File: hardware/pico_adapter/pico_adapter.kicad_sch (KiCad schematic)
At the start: 48 parts, among them J1 L77HDE15SD1CH4F, J2 AudioJack2_Ground, J3 Barrel_Jack, Q1 Q_NMOS_DGS, Q2 Q_NMOS_DGS, U1 DCDC-Module

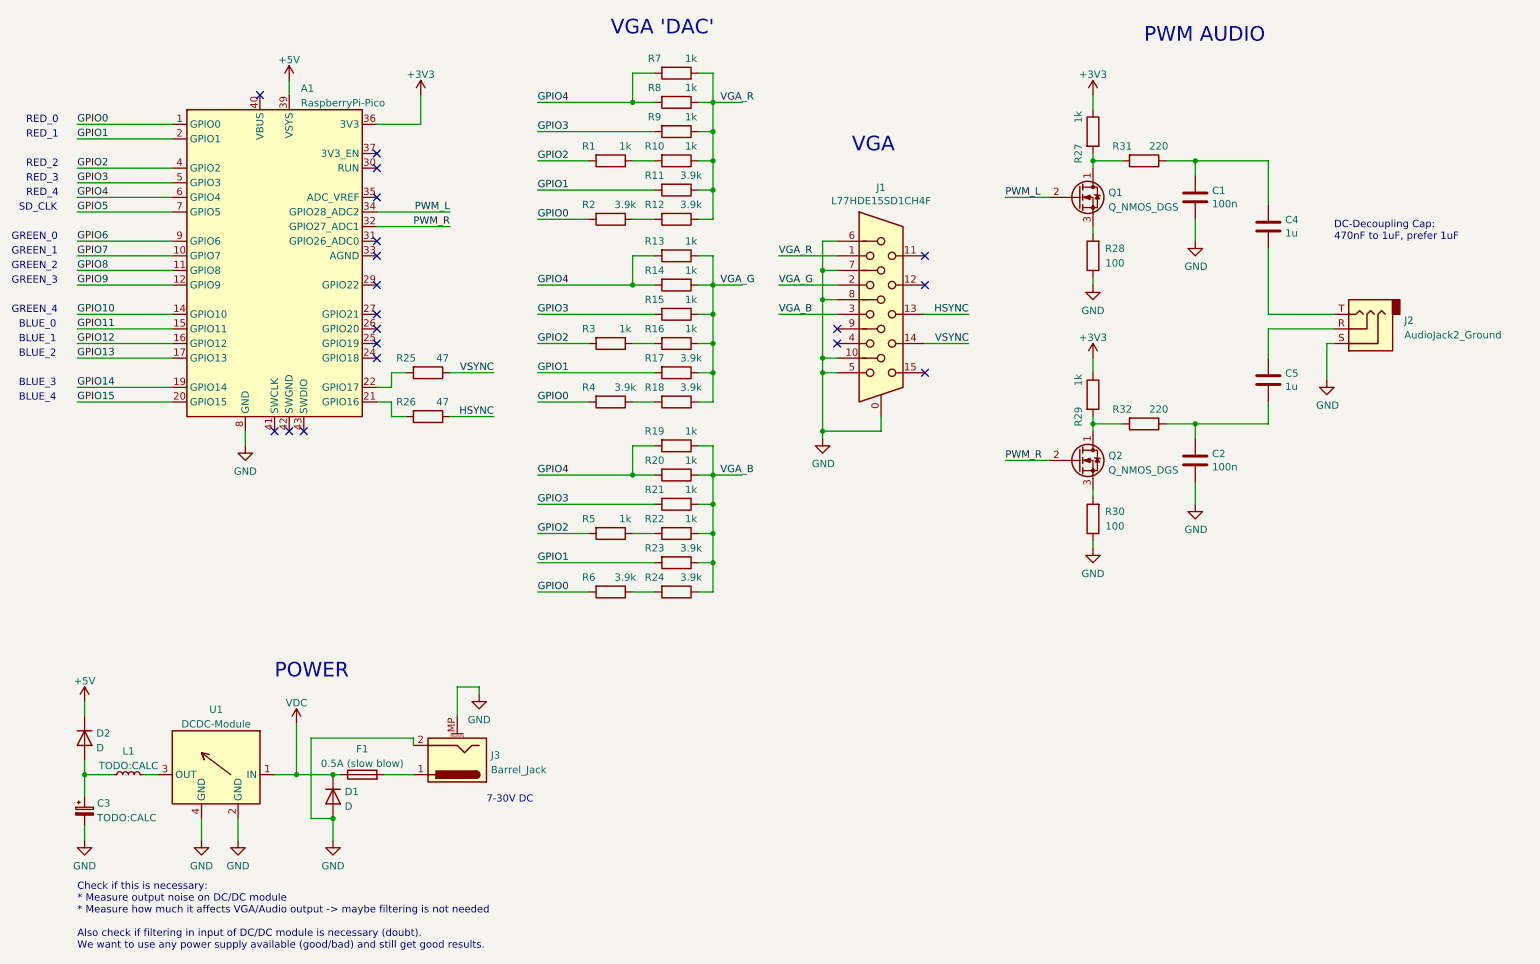
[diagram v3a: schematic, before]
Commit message: simplified PSU only via USB
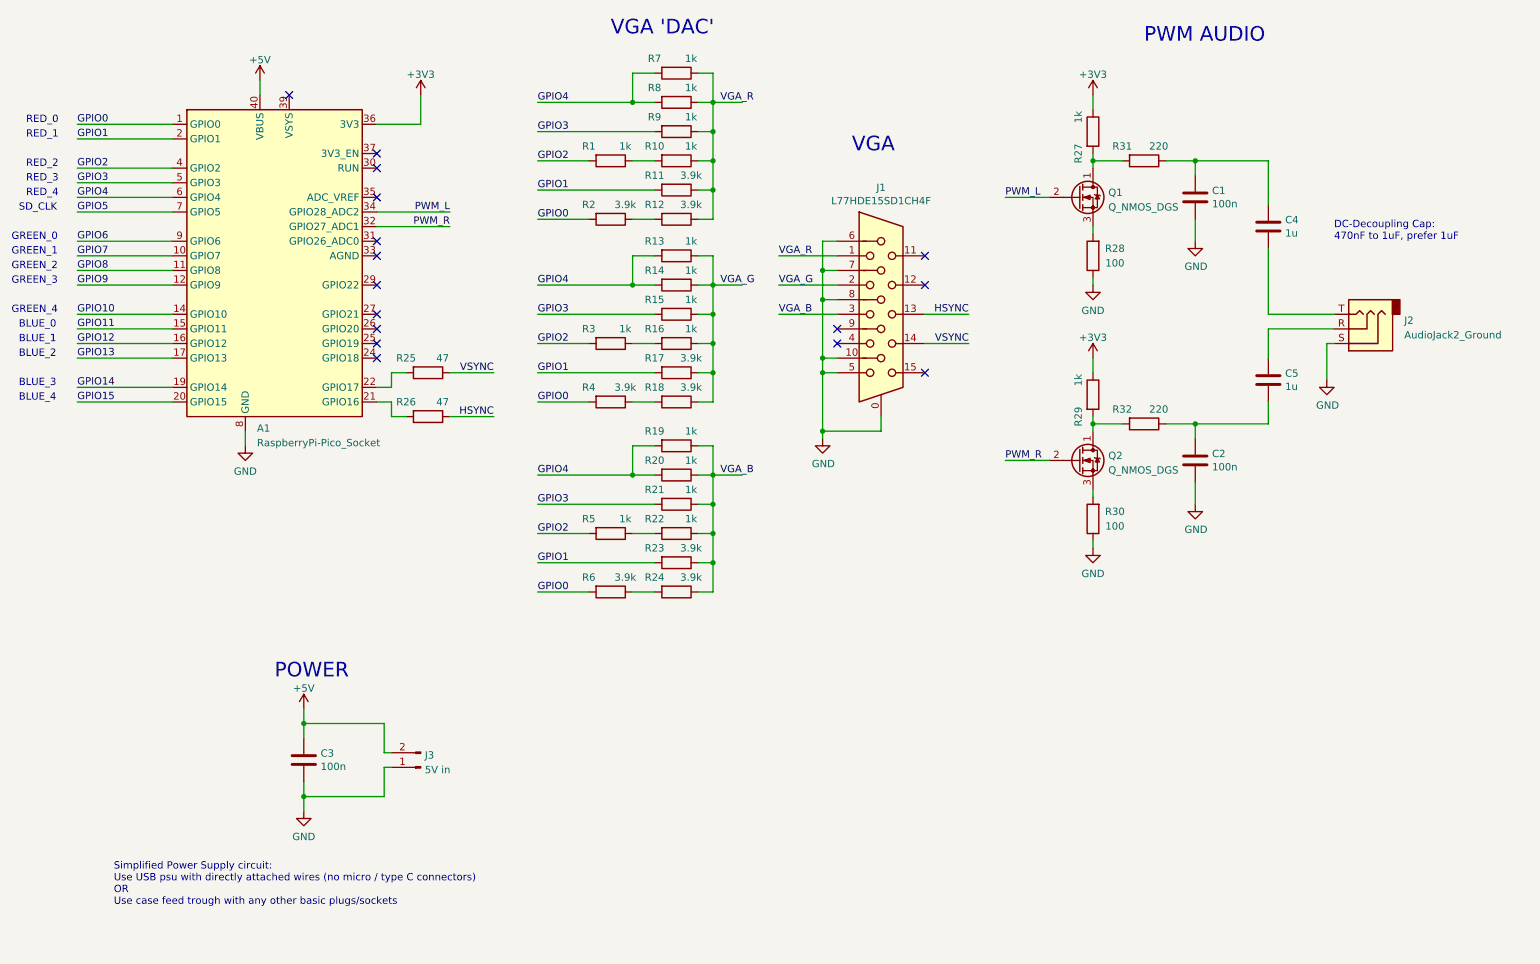
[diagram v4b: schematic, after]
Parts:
- removed A1: RaspberryPi-Pico, Module:Raspberry_Pi_Pico_Socket, symbol PICO_Module:RaspberryPi-Pico
- removed C3: TODO:CALC, Capacitor_THT:CP_Radial_D6.3mm_P2.50mm, symbol Device:C_Polarized_Small
- removed D1, D2: D, Diode_THT:D_A-405_P10.16mm_Horizontal, symbol Device:D
- removed F1: 0.5A (slow blow), Fuse:Fuseholder_Cylinder-5x20mm_Schurter_0031_8201_Horizontal_Open, symbol Device:Fuse
- removed J3: Barrel_Jack, Connector_BarrelJack:BarrelJack_CUI_PJ-102AH_Horizontal, symbol Connector:Barrel_Jack_MountingPin
- removed L1: TODO:CALC, Inductor_THT:L_Radial_D7.5mm_P3.50mm_Fastron_07P, symbol Device:L_Small
- removed U1: DCDC-Module, Module:DCDC-Module, symbol pico_adapter_specific:DCDC-Module
- added A1: RaspberryPi-Pico_Socket, Module:Raspberry_Pi_Pico_Socket, symbol PICO_Module:RaspberryPi-Pico_Socket
- added C3: 100n, Capacitor_THT:C_Rect_L7.5mm_W6.5mm_P5.00mm, symbol Device:C
- added J3: 5V in, Connector_PinHeader_2.54mm:PinHeader_1x02_P2.54mm_Vertical, symbol Connector:Conn_01x02_Male
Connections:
- net +3V3: now also A1.36 (3V3)
- net +5V: now also A1.40 (VBUS), C3.1, J3.2 (Pin_2)
- net GND: now also A1.13 (GND), A1.18 (GND), A1.23 (GND), A1.28 (GND), A1.3 (GND), A1.38 (GND), A1.8 (GND), C3.2, J3.1 (Pin_1)
- net GPIO0: now also A1.1 (GPIO0)
- net GPIO1: now also A1.2 (GPIO1)
- net GPIO10: now also A1.14 (GPIO10)
- net GPIO11: now also A1.15 (GPIO11)
- net GPIO12: now also A1.16 (GPIO12)
- net GPIO13: now also A1.17 (GPIO13)
- net GPIO14: now also A1.19 (GPIO14)
- net GPIO15: now also A1.20 (GPIO15)
- net GPIO2: now also A1.4 (GPIO2)
- net GPIO3: now also A1.5 (GPIO3)
- net GPIO4: now also A1.6 (GPIO4)
- net GPIO5: now also A1.7 (GPIO5)
- net GPIO6: now also A1.9 (GPIO6)
- net GPIO7: now also A1.10 (GPIO7)
- net GPIO8: now also A1.11 (GPIO8)
- net GPIO9: now also A1.12 (GPIO9)
- net PWM_L: now also A1.34 (GPIO28_ADC2)
- net PWM_R: now also A1.32 (GPIO27_ADC1)
- net at R25.2: now also A1.22 (GPIO17)
- net at R26.2: now also A1.21 (GPIO16)
- no-connect marks 19 -> 16
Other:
- note added: "Simplified Power Supply circuit: Use USB psu with directly attached wires (no micro / type C connectors) OR Use case feed trough with any other basic plugs/sockets"
- note removed: "7-30V DC"
- note removed: "Check if this is necessary: * Measure output noise on DC/DC module * Measure how much it affects VGA/Audio output -> maybe filtering is not needed Also check if filtering in input of DC/DC module is necessary (doubt). We want to use any power supply available (good/bad) and still get good results."

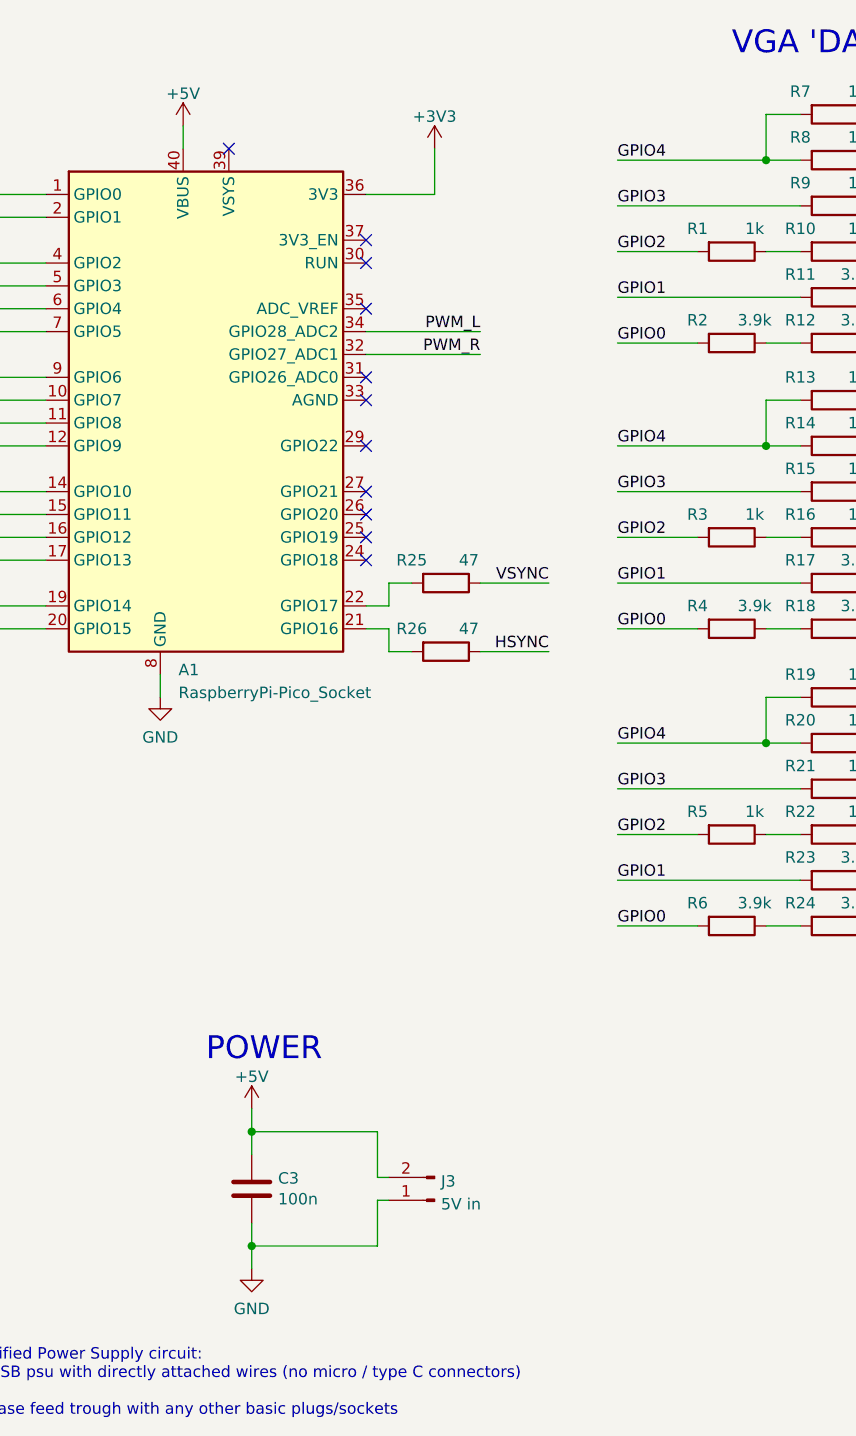
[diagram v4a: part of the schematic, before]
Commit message: fixed PWR_FLAG in schematic, problem: layout GND area does not fill
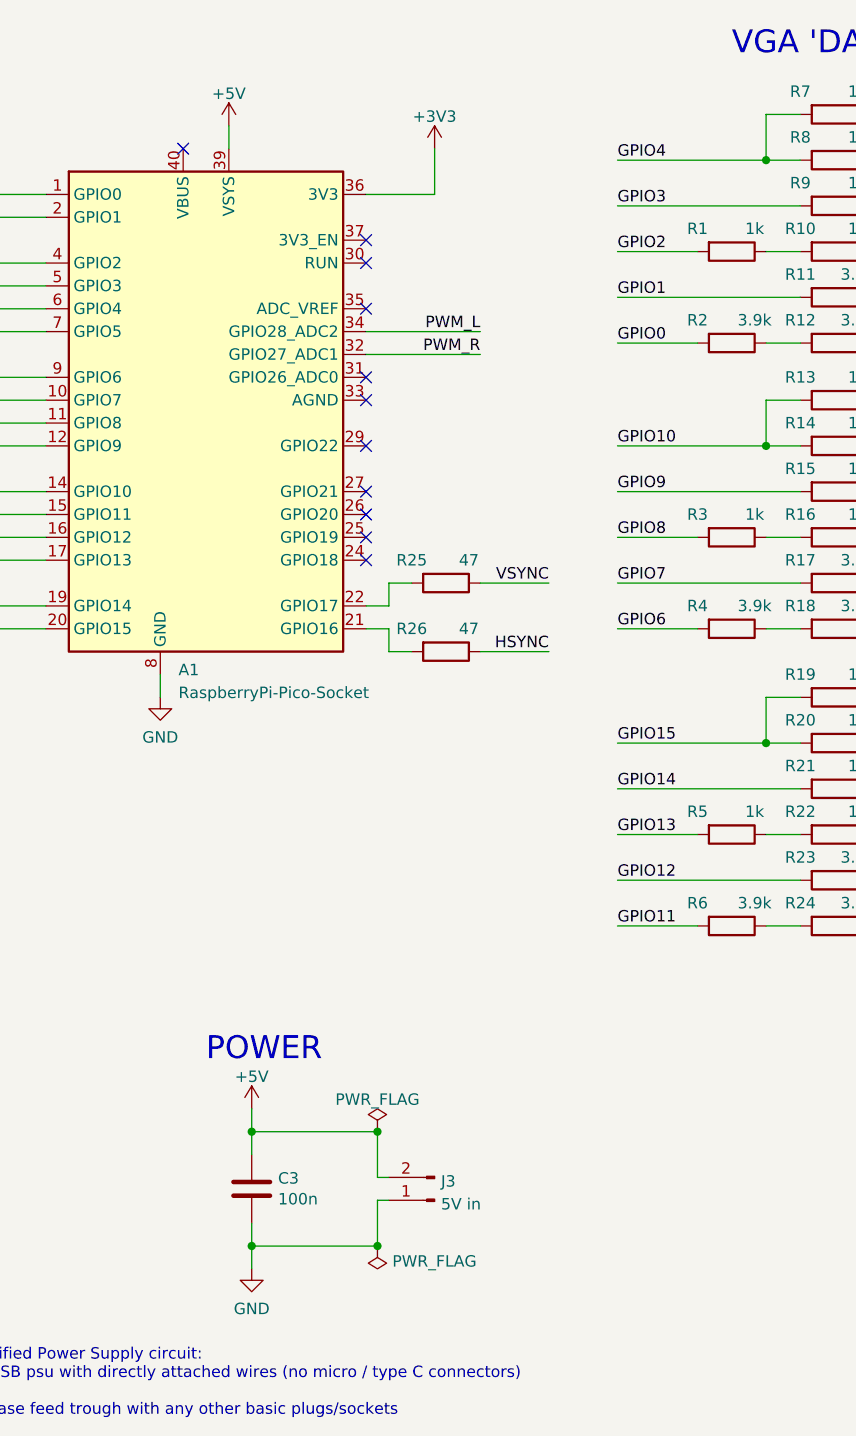
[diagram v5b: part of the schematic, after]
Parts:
- removed A1: RaspberryPi-Pico_Socket, Module:Raspberry_Pi_Pico_Socket, symbol PICO_Module:RaspberryPi-Pico_Socket
- added A1: RaspberryPi-Pico-Socket, Module:Raspberry_Pi_Pico_Socket, symbol PICO_Module:RaspberryPi-Pico-Socket
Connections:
- net +3V3: now also A1.36 (3V3)
- net +5V: now also A1.39 (VSYS)
- net GND: now also A1.13 (GND), A1.18 (GND), A1.23 (GND), A1.28 (GND), A1.3 (GND), A1.38 (GND), A1.8 (GND)
- net GPIO0: now also A1.1 (GPIO0); no longer R4.2, R6.2
- net GPIO1: now also A1.2 (GPIO1); no longer R17.2, R23.2
- net GPIO10: now also R13.2, R14.2, A1.14 (GPIO10)
- net GPIO11: now also R6.2, A1.15 (GPIO11)
- net GPIO12: now also R23.2, A1.16 (GPIO12)
- net GPIO13: now also R5.2, A1.17 (GPIO13)
- net GPIO14: now also R21.2, A1.19 (GPIO14)
- net GPIO15: now also R19.2, R20.2, A1.20 (GPIO15)
- net GPIO2: now also A1.4 (GPIO2); no longer R3.2, R5.2
- net GPIO3: now also A1.5 (GPIO3); no longer R15.2, R21.2
- net GPIO4: now also A1.6 (GPIO4); no longer R13.2, R14.2, R19.2, R20.2
- net GPIO5: now also A1.7 (GPIO5)
- net GPIO6: now also R4.2, A1.9 (GPIO6)
- net GPIO7: now also R17.2, A1.10 (GPIO7)
- net GPIO8: now also R3.2, A1.11 (GPIO8)
- net GPIO9: now also R15.2, A1.12 (GPIO9)
- net PWM_L: now also A1.34 (GPIO28_ADC2)
- net PWM_R: now also A1.32 (GPIO27_ADC1)
- net at R25.2: now also A1.22 (GPIO17)
- net at R26.2: now also A1.21 (GPIO16)

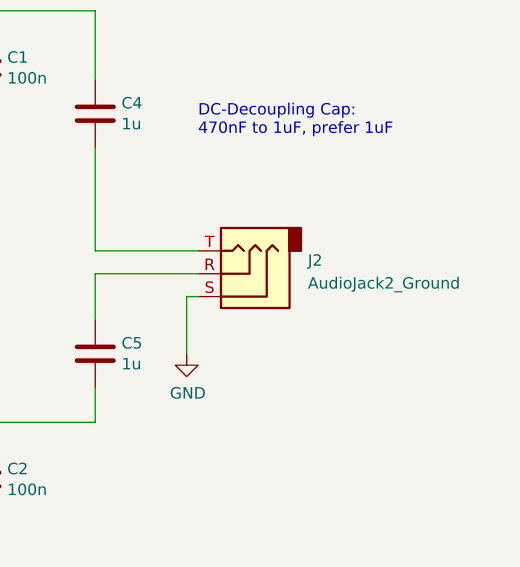
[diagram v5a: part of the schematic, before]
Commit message: GND area does fill now, still DRC errors
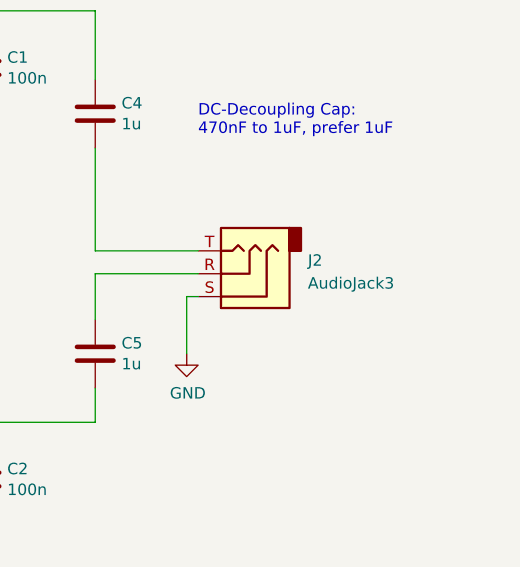
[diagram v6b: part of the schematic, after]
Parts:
- J2: value AudioJack2_Ground -> AudioJack3
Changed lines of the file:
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@@
     (pin "2")
+  )
+  (symbol (lib_id "Connector:AudioJack3") (at 250.19 69.85 180) (unit 1)
+    (in_bom yes) (on_board yes) (fields_autoplaced)
+    (property "Reference" "J2" (id 0) (at 257.302 68.3803 0)
+      (effects (font (size 1.27 1.27)) (justify right))
+    )
+    (property "Value" "AudioJack3" (id 1) (at 257.302 70.9172 0)
+      (effects (font (size 1.27 1.27)) (justify right))
+    )
+    (property "Footprint" "Connector_Audio:Jack_3.5mm_CUI_SJ1-3523N_Horizontal" (id 2) (at 250.19 69.85 0)
+      (effects (font (size 1.27 1.27)) hide)
+    )
+    (property "Datasheet" "~" (id 3) (at 250.19 69.85 0)
+      (effects (font (size 1.27 1.27)) hide)
+    )
+    (pin "R")
+    (pin "S")
+    (pin "T")
   )
   (symbol (lib_id "Device:R") (at 130.81 82.55 270) (unit 1)
@@
     (pin "1")
     (pin "2")
-  )
-  (symbol (lib_id "Connector:AudioJack3") (at 250.19 69.85 180) (unit 1)
-    (in_bom yes) (on_board yes) (fields_autoplaced)
-    (property "Reference" "J2" (id 0) (at 257.302 68.3803 0)
-      (effects (font (size 1.27 1.27)) (justify right))
-    )
-    (property "Value" "AudioJack2_Ground" (id 1) (at 257.302 70.9172 0)
-      (effects (font (size 1.27 1.27)) (justify right))
-    )
-    (property "Footprint" "Connector_Audio:Jack_3.5mm_CUI_SJ1-3523N_Horizontal" (id 2) (at 250.19 69.85 0)
-      (effects (font (size 1.27 1.27)) hide)
-    )
-    (property "Datasheet" "~" (id 3) (at 250.19 69.85 0)
-      (effects (font (size 1.27 1.27)) hide)
-    )
-    (pin "R")
-    (pin "S")
-    (pin "T")
   )
   (symbol (lib_id "power:GND") (at 156.21 88.9 0) (unit 1)
@@
       (reference "J1") (unit 1) (value "L77HDE15SD1CH4F") (footprint "Connector_Dsub:DSUB-15-HD_Female_Horizontal_P2.29x1.98mm_EdgePinOffset8.35mm_Housed_MountingHolesOffset10.89mm")
     )
-    (path "/7093f251-2336-479a-9ce6-b4b1bd05dd80"
-      (reference "J2") (unit 1) (value "AudioJack2_Ground") (footprint "Connector_Audio:Jack_3.5mm_CUI_SJ1-3523N_Horizontal")
+    (path "/25aafccc-32f1-4240-940f-ac8f7092ee50"
+      (reference "J2") (unit 1) (value "AudioJack3") (footprint "Connector_Audio:Jack_3.5mm_CUI_SJ1-3523N_Horizontal")
     )
     (path "/91f8606f-3b82-4295-81ca-4c603721ec24"

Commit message: changed 3.5mm socket
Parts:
- J2: footprint Connector_Audio:Jack_3.5mm_CUI_SJ1-3523N_Horizontal -> Connector_Audio:Jack_3.5mm_CUI_SJ1-3533NG_Horizontal
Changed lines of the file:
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@@
       (effects (font (size 1.27 1.27)) (justify right))
     )
-    (property "Footprint" "Connector_Audio:Jack_3.5mm_CUI_SJ1-3523N_Horizontal" (id 2) (at 250.19 69.85 0)
+    (property "Footprint" "Connector_Audio:Jack_3.5mm_CUI_SJ1-3533NG_Horizontal" (id 2) (at 250.19 69.85 0)
       (effects (font (size 1.27 1.27)) hide)
     )
@@
     )
     (path "/25aafccc-32f1-4240-940f-ac8f7092ee50"
-      (reference "J2") (unit 1) (value "AudioJack3") (footprint "Connector_Audio:Jack_3.5mm_CUI_SJ1-3523N_Horizontal")
+      (reference "J2") (unit 1) (value "AudioJack3") (footprint "Connector_Audio:Jack_3.5mm_CUI_SJ1-3533NG_Horizontal")
     )
     (path "/91f8606f-3b82-4295-81ca-4c603721ec24"
